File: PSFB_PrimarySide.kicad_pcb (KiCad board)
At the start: 2 copper layers, 111 parts, among them Q1 C3M0065100K, Q2 C3M0065100K, Q3 C3M0065100K, Q4 C3M0065100K

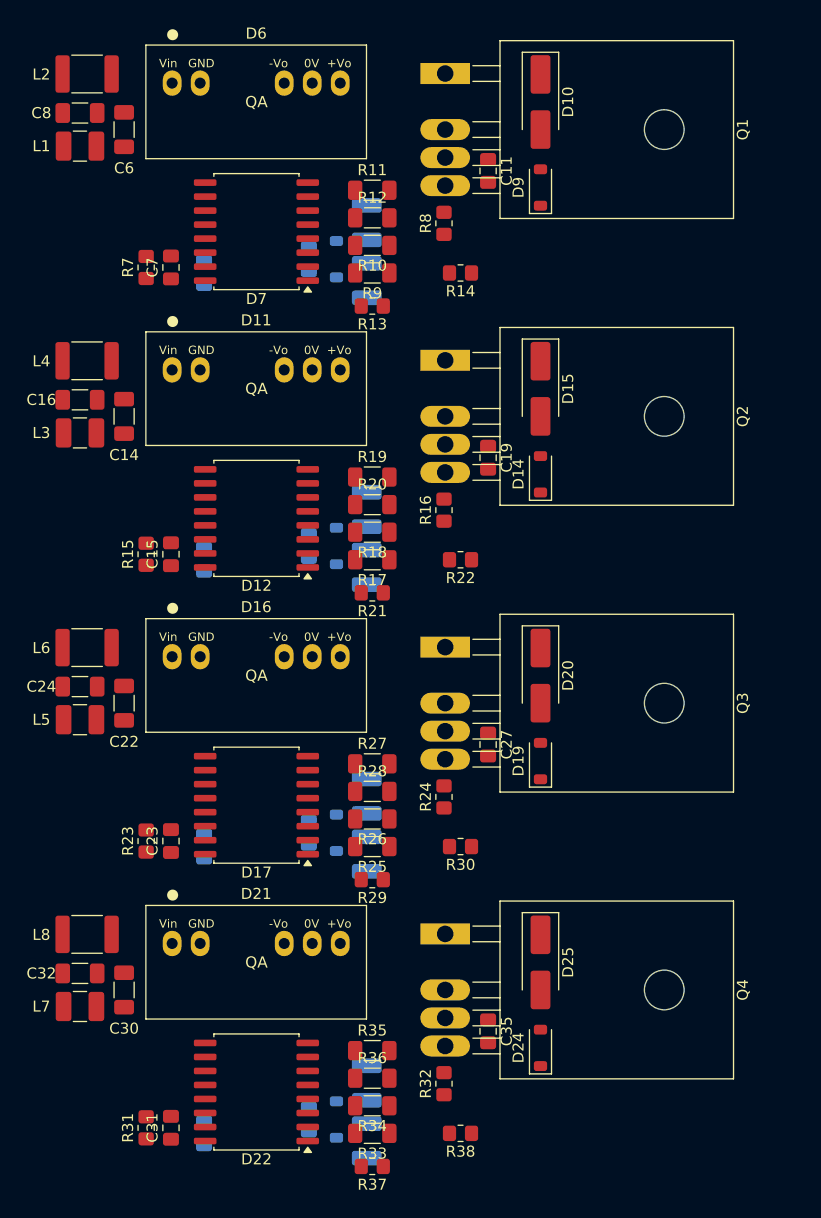
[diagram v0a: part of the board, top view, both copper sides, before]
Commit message: VER1.0: убрал источники с платы
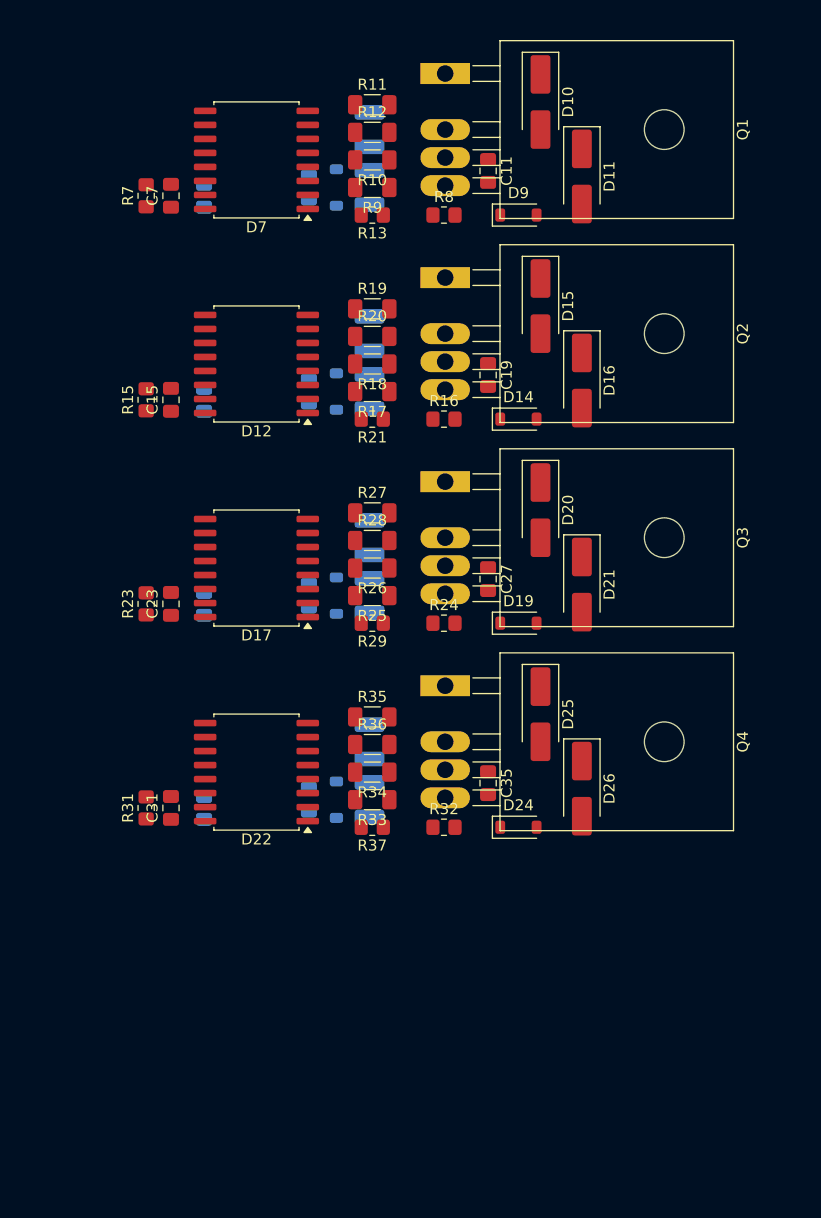
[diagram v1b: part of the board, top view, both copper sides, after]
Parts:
- removed C14, C16, C22, C24, C30, C32, C6, C8: 4.7u, Capacitor_SMD:C_1206_3216Metric_Pad1.33x1.80mm_HandSolder
- removed D6: QA01, MORNSUN:QA01
- removed L1, L3, L5, L7: 12u, Inductor_SMD:L_1210_3225Metric_Pad1.42x2.65mm_HandSolder
- removed L2, L4, L6, L8: 47u, Inductor_SMD:L_1812_4532Metric_Pad1.30x3.40mm_HandSolder
- removed R14, R22, R30, R38: 0, Resistor_SMD:R_0805_2012Metric_Pad1.20x1.40mm_HandSolder
- added D26: ~, Diode_SMD:D_SMA_Handsoldering, F.Cu at (92.2, 140.5)
- D11, D16, D21: value QA01 -> ~; footprint MORNSUN:QA01 -> Diode_SMD:D_SMA_Handsoldering
- moved D21 45.2 mm to (92.2, 122.0), turned to -90 degrees
- moved D16 39.8 mm to (92.2, 103.5), turned to -90 degrees
- moved D11 35.2 mm to (92.2, 85.0), turned to -90 degrees
- moved C33 30.9 mm to (73.0, 136.2)
- moved C34 30.9 mm to (73.0, 141.5)
- moved R37 30.8 mm to (73.2, 144.0)
- moved R33 30.2 mm to (73.2, 141.5)
- moved R34 30.2 mm to (73.2, 139.0)
- moved R35 30.2 mm to (73.2, 134.0)
- moved R36 30.2 mm to (73.2, 136.5)
- moved C29 29.5 mm to (58.0, 142.2)
- moved C31 29.0 mm to (55.0, 142.2)
- moved C36 29.0 mm to (67.5, 141.5)
- moved D22 29.0 mm to (62.8, 139.0)
- moved D23 29.0 mm to (70.0, 141.5)
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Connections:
- C17 pad 1: +15V -> /Driver_2/+15V
- C25 pad 1: +15V -> /Driver_3/+15V
- C33 pad 1: +15V -> /Driver_4/+15V
- C9 pad 1: +15V -> /Driver_1/+15V
- D11 pad 1: Net-(D11-Vin) -> Net-(D10-A)
- D11 pad 2: GND -> Net-(D11-A)
- D12 pad 5: +15V -> /Driver_2/+15V
- D15 pad 2: Net-(D14-A) -> Net-(D15-A)
- D16 pad 1: Net-(D16-Vin) -> Net-(D15-A)
- D16 pad 2: GND -> Net-(D14-A)
- D17 pad 5: +15V -> /Driver_3/+15V
- D20 pad 2: Net-(D19-A) -> Net-(D20-A)
- D21 pad 1: Net-(D21-Vin) -> Net-(D20-A)
- D21 pad 2: GND -> Net-(D19-A)
- D22 pad 5: +15V -> /Driver_4/+15V
- D25 pad 2: Net-(D24-A) -> Net-(D25-A)
- D7 pad 5: +15V -> /Driver_1/+15V
- D9 pad 2: Net-(D10-A) -> Net-(D11-A)
- R13 pad 1: Net-(R13-Pad1) -> Net-(D9-K)
- R21 pad 1: Net-(R21-Pad1) -> Net-(D14-K)
- R29 pad 1: Net-(R29-Pad1) -> Net-(D19-K)
- R37 pad 1: Net-(R37-Pad1) -> Net-(D24-K)

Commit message: VER1.0: добавил разъемы питания
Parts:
- added J1: Supply, Connector_PinSocket_2.54mm:PinSocket_1x03_P2.54mm_Vertical, F.Cu at (65.4, 74.5)
- added J2: Supply, Connector_PinSocket_2.54mm:PinSocket_1x03_P2.54mm_Vertical, F.Cu at (65.4, 93.0)
- added J3: Supply, Connector_PinSocket_2.54mm:PinSocket_1x03_P2.54mm_Vertical, F.Cu at (65.4, 111.5)
- added J4: Supply, Connector_PinSocket_2.54mm:PinSocket_1x03_P2.54mm_Vertical, F.Cu at (65.4, 130.0)

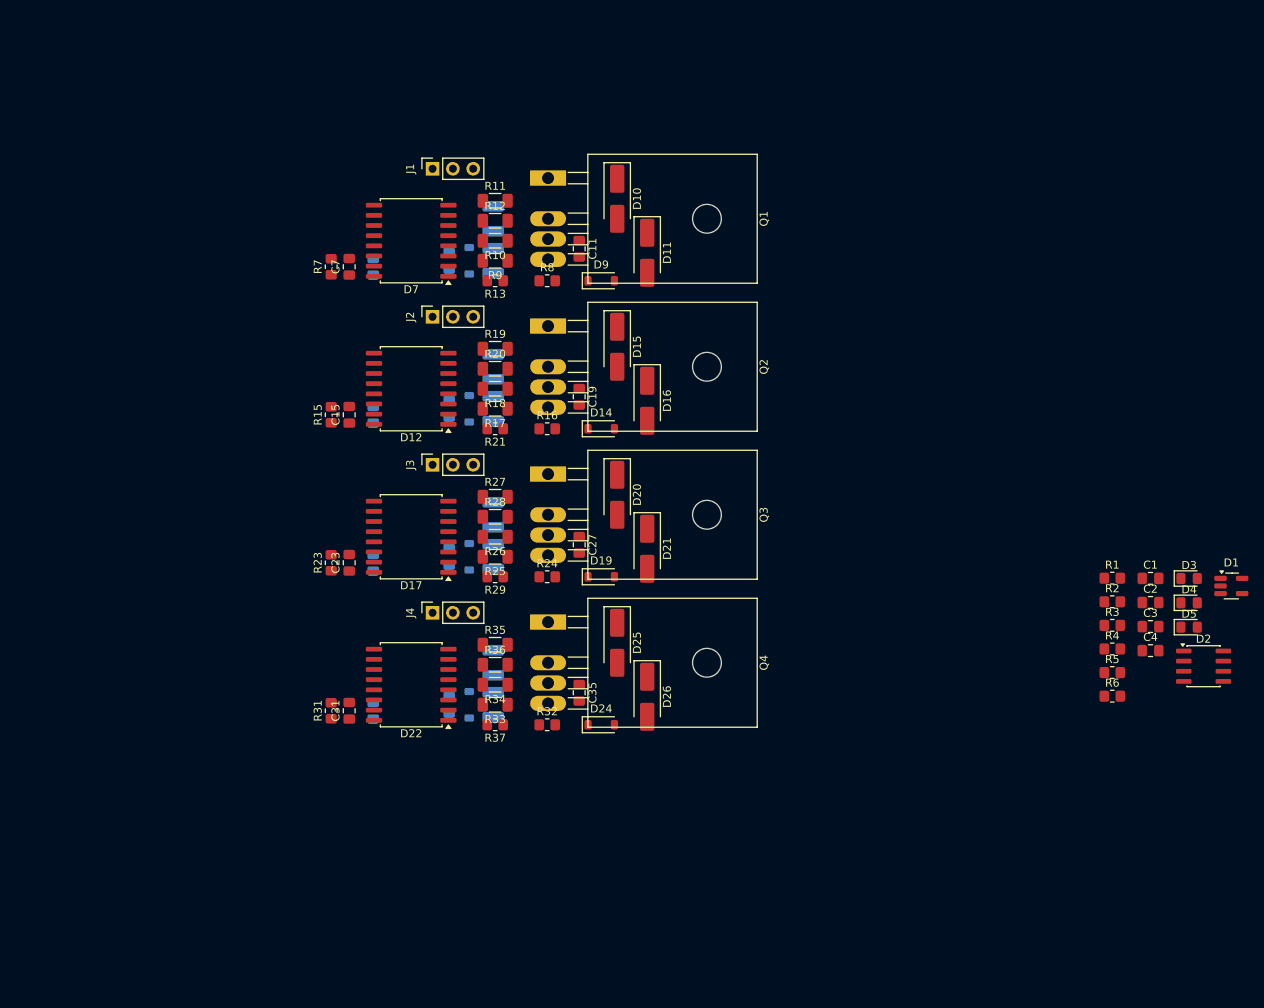
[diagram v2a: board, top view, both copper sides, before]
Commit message: VER1.0: развел 4 канала
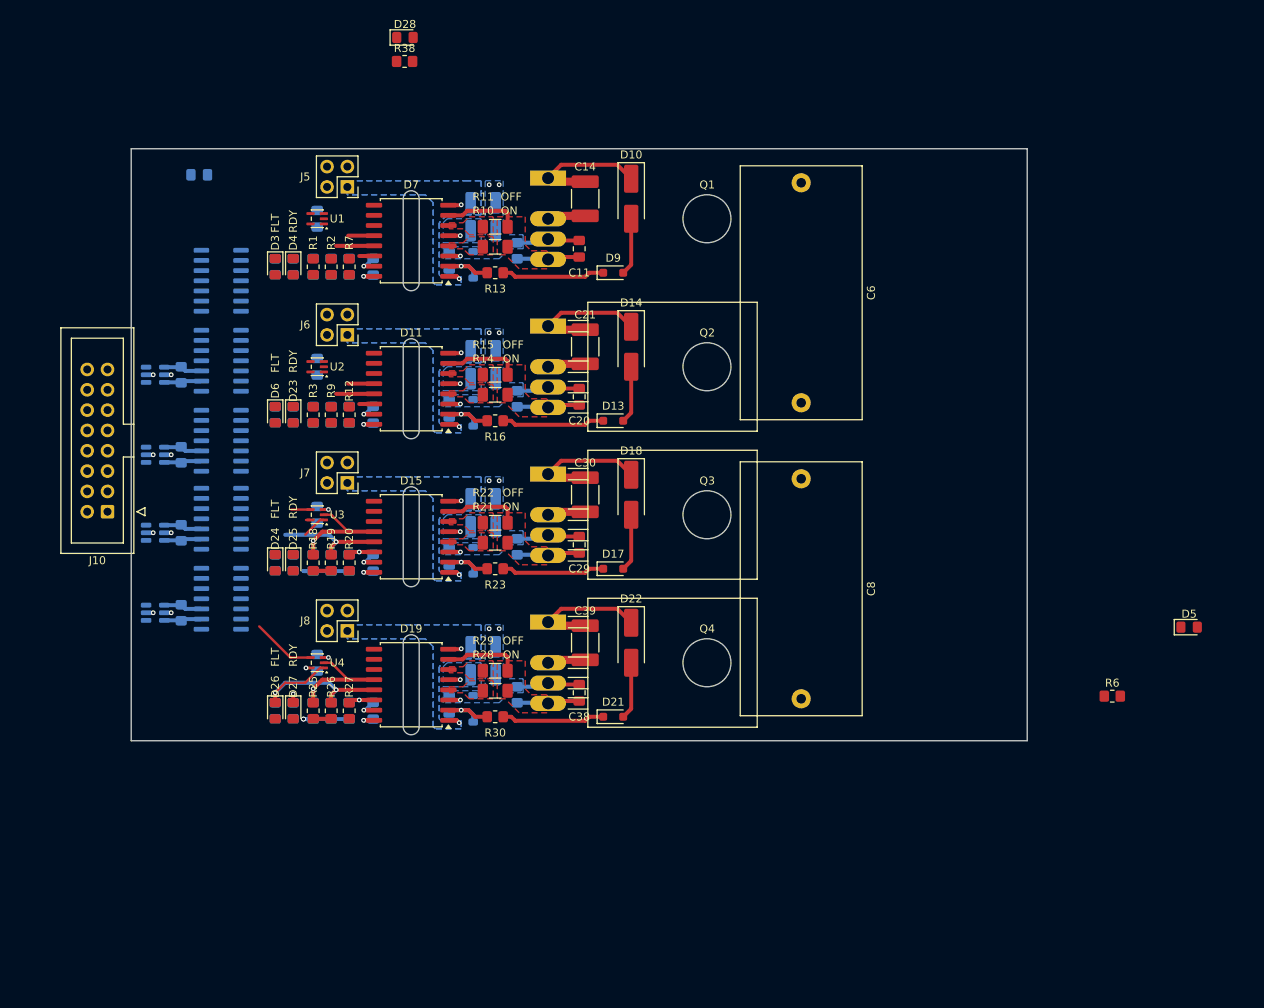
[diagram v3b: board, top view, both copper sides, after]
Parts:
- removed C3: 2.2u, Capacitor_SMD:C_0805_2012Metric_Pad1.18x1.45mm_HandSolder
- removed J1, J2, J3, J4: Supply, Connector_PinSocket_2.54mm:PinSocket_1x03_P2.54mm_Vertical
- added C14: 220p, Capacitor_SMD:C_1812_4532Metric_Pad1.57x3.40mm_HandSolder, F.Cu at (84.5, 78.2)
- added C16: 56p, Capacitor_SMD:C_0805_2012Metric_Pad1.18x1.45mm_HandSolder, B.Cu at (55.0, 105.2)
- added C22: 56p, Capacitor_SMD:C_0805_2012Metric_Pad1.18x1.45mm_HandSolder, B.Cu at (50.5, 123.8)
- added C24: 100n, Capacitor_SMD:C_0805_2012Metric_Pad1.18x1.45mm_HandSolder, B.Cu at (58.0, 123.8)
- added C30: 220p, Capacitor_SMD:C_1812_4532Metric_Pad1.57x3.40mm_HandSolder, F.Cu at (84.5, 115.2)
- added C32: 56p, Capacitor_SMD:C_0805_2012Metric_Pad1.18x1.45mm_HandSolder, B.Cu at (52.8, 142.2)
- added C37: 22p, Capacitor_SMD:C_0805_2012Metric_Pad1.18x1.45mm_HandSolder, B.Cu at (67.5, 141.5)
- added C38: ~, Capacitor_SMD:C_0805_2012Metric_Pad1.18x1.45mm_HandSolder, F.Cu at (83.8, 140.0)
- added C39: 220p, Capacitor_SMD:C_1812_4532Metric_Pad1.57x3.40mm_HandSolder, F.Cu at (84.5, 133.8)
- added C40: 100n, Capacitor_SMD:C_0805_2012Metric_Pad1.18x1.45mm_HandSolder, B.Cu at (51.0, 80.8)
- added C41: 100n, Capacitor_SMD:C_0805_2012Metric_Pad1.18x1.45mm_HandSolder, B.Cu at (51.0, 99.2)
- added C42: 100n, Capacitor_SMD:C_0805_2012Metric_Pad1.18x1.45mm_HandSolder, B.Cu at (51.0, 117.8)
- added C43: 100n, Capacitor_SMD:C_0805_2012Metric_Pad1.18x1.45mm_HandSolder, B.Cu at (51.0, 136.2)
- added C44: 100n, Capacitor_SMD:C_0805_2012Metric_Pad1.18x1.45mm_HandSolder, B.Cu at (36.2, 75.2)
- added C6: 5u, Capacitor_THT:C_Rect_L31.5mm_W15.0mm_P27.50mm_MKS4, F.Cu at (111.5, 76.2)
- added C8: 5u, Capacitor_THT:C_Rect_L31.5mm_W15.0mm_P27.50mm_MKS4, F.Cu at (111.5, 113.2)
- added D27: ~, LED_SMD:LED_0805_2012Metric_Pad1.15x1.40mm_HandSolder, F.Cu at (48.0, 142.2)
- added D28: ~, LED_SMD:LED_0805_2012Metric_Pad1.15x1.40mm_HandSolder, F.Cu at (62.0, 58.1)
- added D29: DS90LV019, Package_SO:SO-14_3.9x8.65mm_P1.27mm, B.Cu at (39.0, 108.5)
- added D30: DS90LV019, Package_SO:SO-14_3.9x8.65mm_P1.27mm, B.Cu at (39.0, 118.2)
- added D31: DS90LV019, Package_SO:SO-14_3.9x8.65mm_P1.27mm, B.Cu at (39.0, 128.2)
- added D6: ~, LED_SMD:LED_0805_2012Metric_Pad1.15x1.40mm_HandSolder, F.Cu at (45.8, 105.2)
- added J10: PSFB_Control, Connector_IDC:IDC-Header_2x08_P2.54mm_Vertical, F.Cu at (24.8, 117.4)
- added J5: Supply, Connector_PinSocket_2.54mm:PinSocket_2x02_P2.54mm_Vertical, F.Cu at (54.8, 76.8)
- added J6: Supply, Connector_PinSocket_2.54mm:PinSocket_2x02_P2.54mm_Vertical, F.Cu at (54.8, 95.3)
- added J7: Supply, Connector_PinSocket_2.54mm:PinSocket_2x02_P2.54mm_Vertical, F.Cu at (54.8, 113.8)
- added J8: Supply, Connector_PinSocket_2.54mm:PinSocket_2x02_P2.54mm_Vertical, F.Cu at (54.8, 132.3)
- added R14: 10, Resistor_SMD:R_1206_3216Metric_Pad1.30x1.75mm_HandSolder, F.Cu at (73.2, 102.8)
- added R22: 2.2, Resistor_SMD:R_1206_3216Metric_Pad1.30x1.75mm_HandSolder, F.Cu at (73.2, 118.8)
- added R30: 100, Resistor_SMD:R_0805_2012Metric_Pad1.20x1.40mm_HandSolder, F.Cu at (73.2, 143.0)
- added R38: 1k, Resistor_SMD:R_0805_2012Metric_Pad1.20x1.40mm_HandSolder, F.Cu at (61.9, 61.1)
- added R39: 100, Resistor_SMD:R_0805_2012Metric_Pad1.20x1.40mm_HandSolder, B.Cu at (34.0, 100.2)
- added R40: 100, Resistor_SMD:R_0805_2012Metric_Pad1.20x1.40mm_HandSolder, B.Cu at (34.0, 110.2)
- added R41: 100, Resistor_SMD:R_0805_2012Metric_Pad1.20x1.40mm_HandSolder, B.Cu at (34.0, 120.0)
- added R42: 100, Resistor_SMD:R_0805_2012Metric_Pad1.20x1.40mm_HandSolder, B.Cu at (34.0, 130.0)
- added U1: 74LVC1G08, Package_TO_SOT_SMD:SOT-353_SC-70-5, F.Cu at (51.0, 80.8)
- added U2: 74LVC1G08, Package_TO_SOT_SMD:SOT-353_SC-70-5, F.Cu at (51.0, 99.2)
- added U3: 74LVC1G08, Package_TO_SOT_SMD:SOT-353_SC-70-5, F.Cu at (51.0, 117.8)
- added U4: 74LVC1G08, Package_TO_SOT_SMD:SOT-353_SC-70-5, F.Cu at (51.0, 136.2)
- added U6: USBLC6-2SC6, Package_TO_SOT_SMD:SOT-23-6, B.Cu at (30.8, 100.2)
- added U7: USBLC6-2SC6, Package_TO_SOT_SMD:SOT-23-6, B.Cu at (30.8, 110.2)
- added U8: USBLC6-2SC6, Package_TO_SOT_SMD:SOT-23-6, B.Cu at (30.8, 120.0)
- added U9: USBLC6-2SC6, Package_TO_SOT_SMD:SOT-23-6, B.Cu at (30.8, 130.0)
- C1, C2, C23, C31, C7, R24, R4, R5, R8: moved to B.Cu
- C12, C28: value 100p -> 22p
- C13: value 100n -> 56p
- C15: value 56p -> 100n; moved to B.Cu
- C19: value ~ -> 22p; moved to B.Cu
- C20: value 100p -> ~; moved to F.Cu
- C21: value 100n -> 220p; footprint Capacitor_SMD:C_0805_2012Metric_Pad1.18x1.45mm_HandSolder -> Capacitor_SMD:C_1812_4532Metric_Pad1.57x3.40mm_HandSolder; moved to F.Cu
- C25, C34: value 10u -> 56p; footprint Capacitor_SMD:C_1210_3225Metric_Pad1.33x2.70mm_HandSolder -> Capacitor_SMD:C_0805_2012Metric_Pad1.18x1.45mm_HandSolder
- C27, C35: value ~ -> 10u; footprint Capacitor_SMD:C_0805_2012Metric_Pad1.18x1.45mm_HandSolder -> Capacitor_SMD:C_1210_3225Metric_Pad1.33x2.70mm_HandSolder; moved to B.Cu
- C29: value 100n -> ~; moved to F.Cu
- C33: value 10u -> 100n; footprint Capacitor_SMD:C_1210_3225Metric_Pad1.33x2.70mm_HandSolder -> Capacitor_SMD:C_0805_2012Metric_Pad1.18x1.45mm_HandSolder
- C36: value 100p -> 10u; footprint Capacitor_SMD:C_0805_2012Metric_Pad1.18x1.45mm_HandSolder -> Capacitor_SMD:C_1210_3225Metric_Pad1.33x2.70mm_HandSolder
- C4: value 2.2u -> 56p; moved to B.Cu
- D1: value ~ -> 74HC21; footprint Package_TO_SOT_SMD:SOT-23-5_HandSoldering -> Package_SO:SOIC-14_3.9x8.7mm_P1.27mm; moved to B.Cu
- D11, D15: value ~ -> NSI6651ASC-DSWR; footprint Diode_SMD:D_SMA_Handsoldering -> Package_SO:SOIC-16W_7.5x10.3mm_P1.27mm
- D12: value NSI6651ASC-DSWR -> ~; footprint Package_SO:SOIC-16W_7.5x10.3mm_P1.27mm -> Diode_SMD:D_SOD-123; moved to B.Cu
- D13: footprint Diode_SMD:D_SOD-123 -> Diode_SMD:D_SOD-323_HandSoldering; moved to F.Cu
- D14: footprint Diode_SMD:D_SOD-123 -> Diode_SMD:D_SMA_Handsoldering
- D16, D20: footprint Diode_SMD:D_SMA_Handsoldering -> Diode_SMD:D_SOD-123; moved to B.Cu
- D17: value NSI6651ASC-DSWR -> ~; footprint Package_SO:SOIC-16W_7.5x10.3mm_P1.27mm -> Diode_SMD:D_SOD-323_HandSoldering
- D18: footprint Diode_SMD:D_SOD-123 -> Diode_SMD:D_SMA_Handsoldering; moved to F.Cu
- D19: value ~ -> NSI6651ASC-DSWR; footprint Diode_SMD:D_SOD-123 -> Package_SO:SOIC-16W_7.5x10.3mm_P1.27mm
- D2: value ~ -> DS90LV019; footprint Package_SO:SOIC-8_3.9x4.9mm_P1.27mm -> Package_SO:SO-14_3.9x8.65mm_P1.27mm; moved to B.Cu
- D21: footprint Diode_SMD:D_SMA_Handsoldering -> Diode_SMD:D_SOD-323_HandSoldering
- D22: value NSI6651ASC-DSWR -> ~; footprint Package_SO:SOIC-16W_7.5x10.3mm_P1.27mm -> Diode_SMD:D_SMA_Handsoldering
- D23: footprint Diode_SMD:D_SOD-123 -> LED_SMD:LED_0805_2012Metric_Pad1.15x1.40mm_HandSolder; moved to F.Cu
- D24: footprint Diode_SMD:D_SOD-123 -> LED_SMD:LED_0805_2012Metric_Pad1.15x1.40mm_HandSolder
- D25, D26: footprint Diode_SMD:D_SMA_Handsoldering -> LED_SMD:LED_0805_2012Metric_Pad1.15x1.40mm_HandSolder
- D9: footprint Diode_SMD:D_SOD-123 -> Diode_SMD:D_SOD-323_HandSoldering
- R10: value 6.8 -> 10
- R11: value 10 -> 2.2
- R12, R20, R27: value 10 -> 120; footprint Resistor_SMD:R_1206_3216Metric_Pad1.30x1.75mm_HandSolder -> Resistor_SMD:R_0805_2012Metric_Pad1.20x1.40mm_HandSolder
- R13: value 2.4k -> 100
- R15: value 120 -> 2.2; footprint Resistor_SMD:R_0805_2012Metric_Pad1.20x1.40mm_HandSolder -> Resistor_SMD:R_1206_3216Metric_Pad1.30x1.75mm_HandSolder
- R16: value 10k -> 100
- R17: value 6.8 -> 10k; footprint Resistor_SMD:R_1206_3216Metric_Pad1.30x1.75mm_HandSolder -> Resistor_SMD:R_0805_2012Metric_Pad1.20x1.40mm_HandSolder; moved to B.Cu
- R18, R25, R26, R9: value 6.8 -> 1k; footprint Resistor_SMD:R_1206_3216Metric_Pad1.30x1.75mm_HandSolder -> Resistor_SMD:R_0805_2012Metric_Pad1.20x1.40mm_HandSolder
- R19: value 10 -> 1k; footprint Resistor_SMD:R_1206_3216Metric_Pad1.30x1.75mm_HandSolder -> Resistor_SMD:R_0805_2012Metric_Pad1.20x1.40mm_HandSolder
- R21: value 2.4k -> 10; footprint Resistor_SMD:R_0805_2012Metric_Pad1.20x1.40mm_HandSolder -> Resistor_SMD:R_1206_3216Metric_Pad1.30x1.75mm_HandSolder
- R23: value 120 -> 100
- R29: value 2.4k -> 2.2; footprint Resistor_SMD:R_0805_2012Metric_Pad1.20x1.40mm_HandSolder -> Resistor_SMD:R_1206_3216Metric_Pad1.30x1.75mm_HandSolder
- R3: value 120 -> 1k
- R31: value 120 -> 10k; moved to B.Cu
- R32: value 10k -> 1k; moved to B.Cu
- R33, R34: value 6.8 -> 1k; footprint Resistor_SMD:R_1206_3216Metric_Pad1.30x1.75mm_HandSolder -> Resistor_SMD:R_0805_2012Metric_Pad1.20x1.40mm_HandSolder; moved to B.Cu
- R35, R36: value 10 -> 1k; footprint Resistor_SMD:R_1206_3216Metric_Pad1.30x1.75mm_HandSolder -> Resistor_SMD:R_0805_2012Metric_Pad1.20x1.40mm_HandSolder; moved to B.Cu
- R37: value 2.4k -> 1k; moved to B.Cu
- moved D1 131.9 mm to (39.0, 88.5), turned to 180 degrees
- moved D2 128.6 mm to (39.0, 98.5), turned to 180 degrees
- moved D3 120.7 mm to (45.8, 86.8), turned to -90 degrees
- moved D4 119.6 mm to (48.0, 86.8), turned to -90 degrees
- moved R4 115.0 mm to (45.8, 86.8), turned to 90 degrees
- moved R5 114.3 mm to (48.0, 86.8), turned to 90 degrees
- moved C1 111.7 mm to (50.5, 86.8), turned to -90 degrees
- moved C2 110.7 mm to (52.8, 86.8), turned to -90 degrees
- moved C4 108.7 mm to (50.5, 105.2), turned to -90 degrees
- moved R1 107.2 mm to (50.5, 86.8), turned to -90 degrees
- moved R2 106.2 mm to (52.8, 86.8), turned to -90 degrees
- moved R3 103.3 mm to (50.5, 105.2), turned to -90 degrees
- moved R32 51.6 mm to (45.8, 105.2), turned to 90 degrees
- moved D26 46.5 mm to (45.8, 142.2)
- moved D24 45.5 mm to (45.8, 123.8), turned to -90 degrees
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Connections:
- C1 pad 1: RDY_A -> /Driver_1/RDY
- C13 pad 1: GND -> /Driver_2/~{FLT}
- C13 pad 2: +5V -> GND
- C15 pad 2: Net-(D12-~{RST}) -> +5V
- C17 pad 2: /Driver_2/GND2 -> GNDPWR
- C18 pad 1: /Driver_2/GND2 -> GNDPWR
- C19 pad 1: /Driver_2/GND2 -> Net-(D11-DESAT)
- C19 pad 2: Net-(D12-CLAMP) -> GNDPWR
- C2 pad 1: FLT_A -> /Driver_1/~{FLT}
- C20 pad 1: Net-(D12-DESAT) -> GNDPWR
- C20 pad 2: /Driver_2/GND2 -> Net-(D11-CLAMP)
- C21 pad 1: GND -> /Driver_1/GND2
- C21 pad 2: +5V -> GNDPWR
- C23 pad 1: GND -> /Driver_3/~{FLT}
- C23 pad 2: Net-(D17-~{RST}) -> GND
- C25 pad 1: /Driver_3/+15V -> GND
- C25 pad 2: /Driver_3/GND2 -> Net-(D15-~{RST})
- C26 pad 1: /Driver_3/GND2 -> /Driver_3/+15V
- C26 pad 2: /Driver_3/-4V -> /Driver_3/GND2
- C27 pad 2: Net-(D17-CLAMP) -> /Driver_3/-4V
- C28 pad 1: Net-(D17-DESAT) -> Net-(D15-DESAT)
- C29 pad 1: GND -> /Driver_3/GND2
- C29 pad 2: +5V -> Net-(D15-CLAMP)
- C31 pad 1: GND -> /Driver_4/RDY
- C31 pad 2: Net-(D22-~{RST}) -> GND
- C33 pad 1: /Driver_4/+15V -> GND
- C33 pad 2: /Driver_4/GND2 -> +5V
- C34 pad 1: /Driver_4/GND2 -> GND
- C34 pad 2: /Driver_4/-4V -> Net-(D19-~{RST})
- C35 pad 1: /Driver_4/GND2 -> /Driver_4/+15V
- C35 pad 2: Net-(D22-CLAMP) -> GNDPWR
- C36 pad 1: Net-(D22-DESAT) -> GNDPWR
- C36 pad 2: /Driver_4/GND2 -> /Driver_4/-4V
- C4 pad 1: +5V -> /Driver_2/RDY
- D1 pad 1: FLT_A -> /Common_FLT4
- D1 pad 2: RDY_A -> /Common_FLT3
- D1 pad 3: GND -> unconnected-(D1-NC-Pad3)
- D1 pad 4: Net-(D1-Y) -> /Common_FLT2
- D1 pad 5: +5V -> /Common_FLT1
- D10 pad 1: /Driver_1/Drain_PWR -> VDC
- D11 pad 1: Net-(D10-A) -> /Driver_2/-4V
- D11 pad 2: Net-(D11-A) -> Net-(D11-DESAT)
- D12 pad 1: /Driver_2/-4V -> Net-(D11-DESAT)
- D12 pad 2: Net-(D12-DESAT) -> GNDPWR
- D13 pad 1: Net-(D12-DESAT) -> Net-(D13-K)
- D13 pad 2: /Driver_2/GND2 -> Net-(D13-A)
- D14 pad 1: Net-(D14-K) -> /Driver_1/GND2
- D14 pad 2: Net-(D14-A) -> Net-(D13-A)
- D15 pad 1: /Driver_2/Drain_PWR -> /Driver_3/-4V
- D15 pad 2: Net-(D15-A) -> Net-(D15-DESAT)
- D16 pad 1: Net-(D15-A) -> Net-(D15-DESAT)
- D16 pad 2: Net-(D14-A) -> /Driver_3/GND2
- D17 pad 1: /Driver_3/-4V -> Net-(D17-K)
- D17 pad 2: Net-(D17-DESAT) -> Net-(D17-A)
- D18 pad 1: Net-(D17-DESAT) -> VDC
- D18 pad 2: /Driver_3/GND2 -> Net-(D17-A)
- D19 pad 1: Net-(D19-K) -> /Driver_4/-4V
- D19 pad 2: Net-(D19-A) -> Net-(D19-DESAT)
- D2 pad 1: unconnected-(D2-RO-Pad1) -> GND
- D2 pad 2: +5V -> unconnected-(D2-DIN-Pad2)
- D2 pad 3: +5V -> (no net)
- D2 pad 4: Net-(D1-Y) -> /PWM_H1
- D2 pad 5: GND -> (no net)
- D2 pad 6: ERR_A_P -> (no net)
- D2 pad 7: ERR_A_N -> GND
- D2 pad 8: +5V -> GND
- D20 pad 1: /Driver_3/Drain_PWR -> Net-(D19-DESAT)
- D20 pad 2: Net-(D20-A) -> GNDPWR
- D21 pad 1: Net-(D20-A) -> Net-(D21-K)
- D21 pad 2: Net-(D19-A) -> Net-(D21-A)
- D22 pad 1: /Driver_4/-4V -> /Driver_3/GND2
- D22 pad 2: Net-(D22-DESAT) -> Net-(D21-A)
- D23 pad 1: Net-(D22-DESAT) -> GND
- D23 pad 2: /Driver_4/GND2 -> Net-(D23-A)
- D24 pad 1: Net-(D24-K) -> /Driver_3/~{FLT}
- D25 pad 1: /Driver_4/Drain_PWR -> GND
- D26 pad 1: Net-(D25-A) -> /Driver_4/~{FLT}
- D26 pad 2: Net-(D24-A) -> Net-(D26-A)
- D3 pad 1: FLT_A -> /Driver_1/~{FLT}
- D7 pad 10: /Driver_1/PWM_IN+ -> /PWM_H1
- D7 pad 11: /Driver_1/PWM_IN- -> /PWM_L1
- D9 pad 2: Net-(D11-A) -> Net-(D10-A)
- Q1 pad 1: /Driver_1/Drain_PWR -> VDC
- Q1 pad 2: /Driver_1/Source_PWR -> /Driver_1/GND2
- Q2 pad 1: /Driver_2/Drain_PWR -> /Driver_1/GND2
- Q2 pad 2: /Driver_2/Source_PWR -> GNDPWR
- Q2 pad 3: /Driver_2/GND2 -> GNDPWR
- Q2 pad 4: Net-(D12-CLAMP) -> Net-(D11-CLAMP)
- Q3 pad 1: /Driver_3/Drain_PWR -> VDC
- Q3 pad 2: /Driver_3/Source_PWR -> /Driver_3/GND2
- Q3 pad 4: Net-(D17-CLAMP) -> Net-(D15-CLAMP)
- Q4 pad 1: /Driver_4/Drain_PWR -> /Driver_3/GND2
- Q4 pad 2: /Driver_4/Source_PWR -> GNDPWR
- Q4 pad 3: /Driver_4/GND2 -> GNDPWR
- Q4 pad 4: Net-(D22-CLAMP) -> Net-(D19-CLAMP)
- R1 pad 1: RDY_A -> /Driver_1/RDY
- R12 pad 1: Net-(D7-OUTL) -> /RST
- R12 pad 2: Net-(D7-CLAMP) -> Net-(D11-~{RST})
- R15 pad 1: /Driver_2/~{RST} -> Net-(D11-OUTL)
- R15 pad 2: Net-(D12-~{RST}) -> Net-(D11-CLAMP)
- R16 pad 1: /Driver_2/GND2 -> Net-(D13-K)
- R16 pad 2: Net-(D12-CLAMP) -> Net-(D11-DESAT)
- R17 pad 1: Net-(D12-CLAMP) -> GNDPWR
- R17 pad 2: Net-(D12-OUTH) -> Net-(D11-CLAMP)
- R18 pad 1: Net-(D12-CLAMP) -> /Driver_3/RDY
- R18 pad 2: Net-(D12-OUTH) -> +5V
- R19 pad 1: Net-(D12-OUTL) -> /Driver_3/~{FLT}
- R19 pad 2: Net-(D12-CLAMP) -> +5V
- R2 pad 1: FLT_A -> /Driver_1/~{FLT}
- R20 pad 1: Net-(D12-OUTL) -> /RST
- R20 pad 2: Net-(D12-CLAMP) -> Net-(D15-~{RST})
- R21 pad 1: Net-(D14-K) -> Net-(D15-CLAMP)
- R21 pad 2: Net-(D12-DESAT) -> Net-(D15-OUTH)
- R23 pad 1: /Driver_3/~{RST} -> Net-(D17-K)
- R23 pad 2: Net-(D17-~{RST}) -> Net-(D15-DESAT)
- R24 pad 2: Net-(D17-CLAMP) -> Net-(D15-CLAMP)
- R25 pad 1: Net-(D17-CLAMP) -> /Driver_4/RDY
- R25 pad 2: Net-(D17-OUTH) -> +5V
- R26 pad 1: Net-(D17-CLAMP) -> /Driver_4/~{FLT}
- R26 pad 2: Net-(D17-OUTH) -> +5V
- R27 pad 1: Net-(D17-OUTL) -> /RST
- R27 pad 2: Net-(D17-CLAMP) -> Net-(D19-~{RST})
- R28 pad 1: Net-(D17-OUTL) -> Net-(D19-CLAMP)
- R28 pad 2: Net-(D17-CLAMP) -> Net-(D19-OUTH)
- R29 pad 1: Net-(D19-K) -> Net-(D19-OUTL)
- R29 pad 2: Net-(D17-DESAT) -> Net-(D19-CLAMP)
- R3 pad 1: ERR_A_N -> /Driver_2/RDY
- R3 pad 2: ERR_A_P -> +5V
- R31 pad 1: /Driver_4/~{RST} -> GNDPWR
- R31 pad 2: Net-(D22-~{RST}) -> Net-(D19-CLAMP)
- R32 pad 1: /Driver_4/GND2 -> Net-(D6-A)
- R32 pad 2: Net-(D22-CLAMP) -> +5V
- R33 pad 1: Net-(D22-CLAMP) -> Net-(D23-A)
- R33 pad 2: Net-(D22-OUTH) -> /Driver_2/RDY
- R34 pad 1: Net-(D22-CLAMP) -> Net-(D24-A)
- R34 pad 2: Net-(D22-OUTH) -> +5V
- R35 pad 1: Net-(D22-OUTL) -> Net-(D25-A)
- R35 pad 2: Net-(D22-CLAMP) -> /Driver_3/RDY
- R36 pad 1: Net-(D22-OUTL) -> Net-(D26-A)
- R36 pad 2: Net-(D22-CLAMP) -> +5V
- R37 pad 1: Net-(D24-K) -> Net-(D27-A)
- R37 pad 2: Net-(D22-DESAT) -> /Driver_4/RDY
- R5 pad 2: RDY_A -> /Driver_1/RDY
- R7 pad 1: /Driver_1/~{RST} -> /RST
- R9 pad 1: Net-(D7-CLAMP) -> /Driver_2/~{FLT}
- R9 pad 2: Net-(D7-OUTH) -> +5V
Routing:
- net VDC: track 0.00 -> 32.0 mm
- net /Driver_1/GND2: track 0.00 -> 28.9 mm, vias 0 -> 3
- net /Driver_3/GND2: track 0.00 -> 28.9 mm, vias 0 -> 3
- net GND: track 0.00 -> 28.8 mm, vias 0 -> 13
- net GNDPWR: track 0.00 -> 25.8 mm, vias 0 -> 6
- net /Driver_4/~{FLT}: track 0.00 -> 25.5 mm, vias 0 -> 2
- net +5V: track 0.00 -> 20.6 mm, vias 0 -> 9
- net /Driver_3/~{FLT}: track 0.00 -> 18.3 mm, vias 0 -> 1
- net Net-(D7-CLAMP): track 0.00 -> 16.8 mm
- net Net-(D15-CLAMP): track 0.00 -> 16.8 mm
- net Net-(D11-CLAMP): track 0.00 -> 16.8 mm
- net Net-(D19-CLAMP): track 0.00 -> 16.8 mm
- net /Driver_4/RDY: track 0.00 -> 15.7 mm, vias 0 -> 1
- net /Driver_3/RDY: track 0.00 -> 15.6 mm, vias 0 -> 1
- net Net-(D9-K): track 0.00 -> 12.9 mm
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- added copper zone on In1.Cu, net (none)
- added copper zone on B.Cu, net /Driver_1/+15V
- added copper zone on In2.Cu, net /Driver_1/+15V
- added copper zone on B.Cu, net /Driver_1/-4V
- added copper zone on B.Cu, net /Driver_1/GND2
- added copper zone on In1.Cu, net /Driver_1/GND2
- added copper zone on B.Cu, net /Driver_2/+15V
- added copper zone on In2.Cu, net /Driver_2/+15V
- added copper zone on B.Cu, net /Driver_2/-4V
- added copper zone on B.Cu, net /Driver_3/+15V
- added copper zone on In2.Cu, net /Driver_3/+15V
- added copper zone on B.Cu, net /Driver_3/-4V
- added copper zone on B.Cu, net /Driver_3/GND2
- added copper zone on In1.Cu, net /Driver_3/GND2
- added copper zone on B.Cu, net /Driver_4/+15V
- added copper zone on In2.Cu, net /Driver_4/+15V
- added copper zone on B.Cu, net /Driver_4/-4V
- added copper zone on B.Cu, net GNDPWR
- added copper zone on In1.Cu, net GNDPWR
- added copper zone on In2.Cu, net GNDPWR
- added copper zone on F.Cu, net Net-(D11-CLAMP)
- added copper zone on F.Cu, net Net-(D11-OUTH)
- added copper zone on F.Cu, net Net-(D11-OUTL)
- added copper zone on F.Cu, net Net-(D15-CLAMP)
- added copper zone on F.Cu, net Net-(D15-OUTH)
- added copper zone on F.Cu, net Net-(D15-OUTL)
- added copper zone on F.Cu, net Net-(D19-CLAMP)
- added copper zone on F.Cu, net Net-(D19-OUTH)
- added copper zone on F.Cu, net Net-(D19-OUTL)
- added copper zone on F.Cu, net Net-(D7-CLAMP)
- added copper zone on F.Cu, net Net-(D7-OUTH)
- added copper zone on F.Cu, net Net-(D7-OUTL)
- added copper zone on In1.Cu, net VDC
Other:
- board outline added: 112 x 74 mm
- copper layers 2 -> 4
- board text added: "FLT"
- board text added: "OFF"
- board text added: "ON"
- board text added: "RDY"
